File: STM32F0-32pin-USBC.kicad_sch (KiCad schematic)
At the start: 0 parts

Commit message: Added kicad_hugonlib submodule and added libs to project
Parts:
- added H1, H2, H3, H4: MountingHole, symbol Mechanical:MountingHole
- added J1: Conn_ARM_JTAG_SWD_10, symbol Connector:Conn_ARM_JTAG_SWD_10
- added J2: USB_C_Receptacle_USB2.0_16P, symbol Connector:USB_C_Receptacle_USB2.0_16P
- added U1: USBLC6-2SC6, Package_TO_SOT_SMD:SOT-23-6, symbol Power_Protection:USBLC6-2SC6
- added U2: STM32F042K6Tx, Package_QFP:LQFP-32_7x7mm_P0.8mm, symbol MCU_ST_STM32F0:STM32F042K6Tx
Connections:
- new net: J1.3 (GND), J1.5 (GND)
- new net: J2.A1 (GND), J2.A12 (GND), J2.B1 (GND), J2.B12 (GND)
- new net: J2.A4 (VBUS), J2.A9 (VBUS), J2.B4 (VBUS), J2.B9 (VBUS)

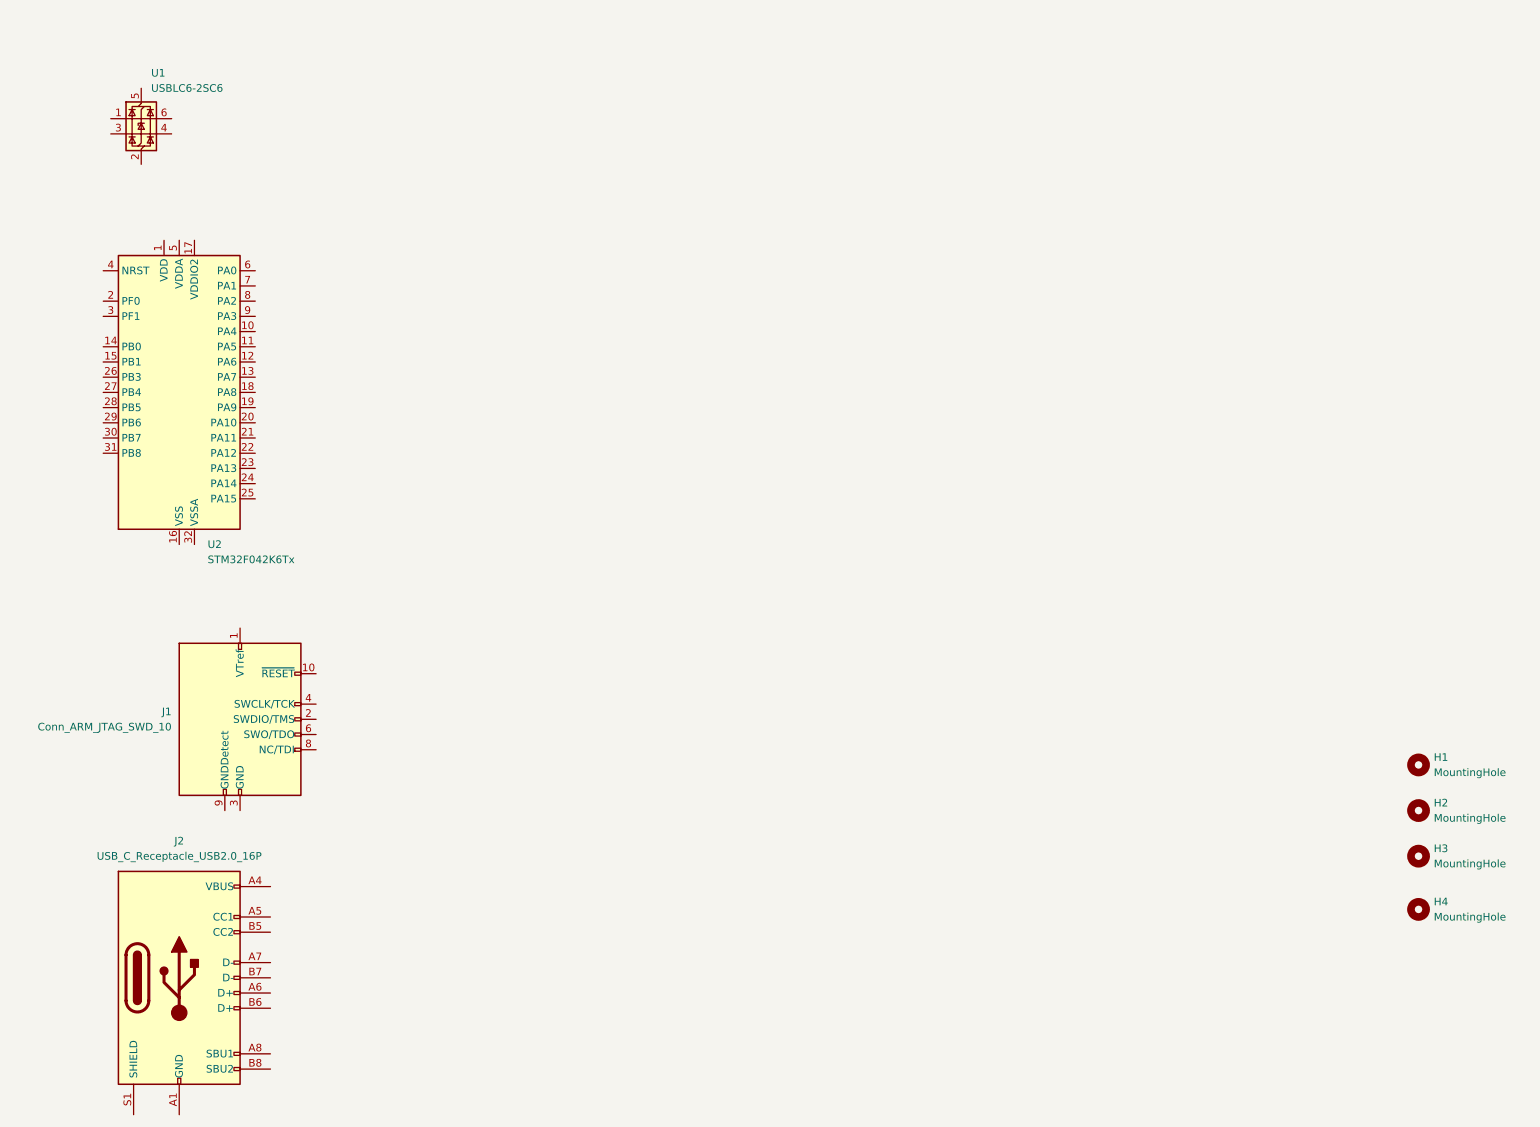
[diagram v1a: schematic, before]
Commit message: Added symbols and completed USB_and_LDO sheet
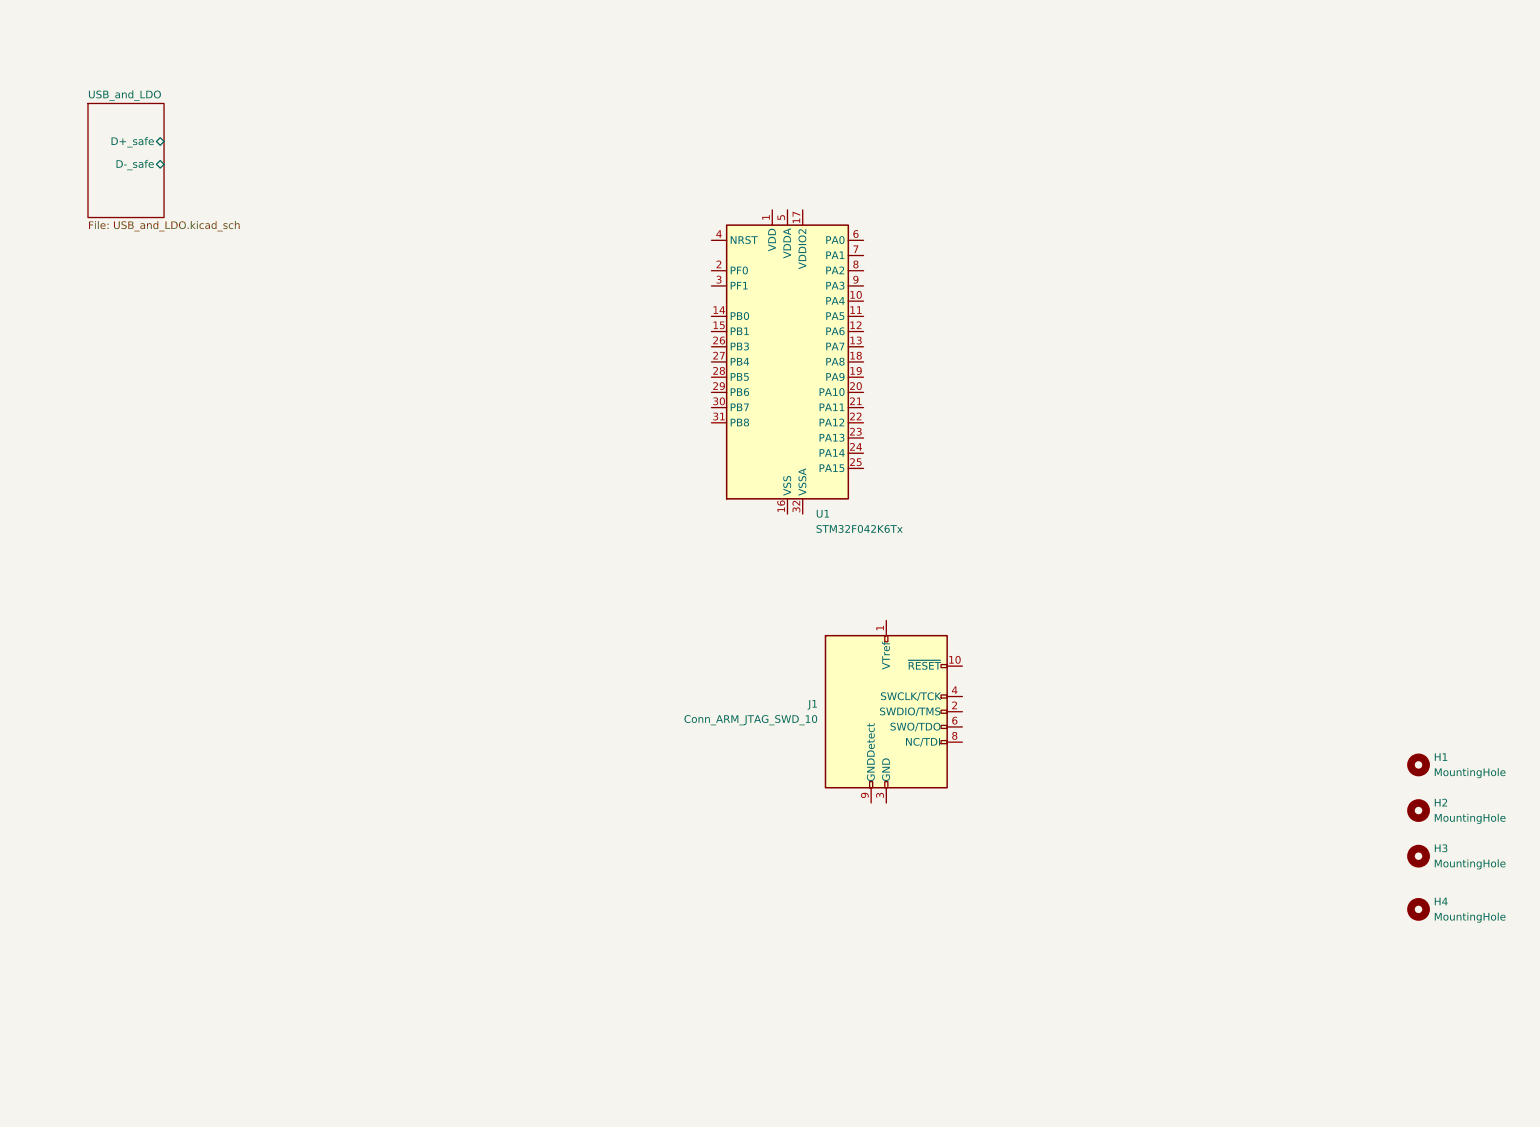
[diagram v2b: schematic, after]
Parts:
- removed J2: USB_C_Receptacle_USB2.0_16P, symbol Connector:USB_C_Receptacle_USB2.0_16P
- removed U1: USBLC6-2SC6, Package_TO_SOT_SMD:SOT-23-6, symbol Power_Protection:USBLC6-2SC6
- renumbered U2 to U1
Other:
- added sheet USB_and_LDO (USB_and_LDO.kicad_sch)
- moved on the sheet: J1, U1
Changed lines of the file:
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@@
-	)
-	(symbol
-		(lib_id "Power_Protection:USBLC6-2SC6")
-		(at 34.29 33.02 0)
-		(unit 1)
-		(exclude_from_sim no)
-		(in_bom yes)
-		(on_board yes)
-		(dnp no)
-		(fields_autoplaced yes)
-		(property "Reference" "U1"
-			(at 35.9411 25.4 0)
-			(effects
-				(font
-					(size 1.27 1.27)
-				)
-				(justify left)
-			)
-		)
-		(property "Value" "USBLC6-2SC6"
-			(at 35.9411 27.94 0)
-			(effects
-				(font
-					(size 1.27 1.27)
-				)
-				(justify left)
-			)
-		)
-		(property "Footprint" "Package_TO_SOT_SMD:SOT-23-6"
-			(at 35.56 39.37 0)
-			(effects
-				(font
-					(size 1.27 1.27)
-					(italic yes)
-				)
-				(justify left)
-				(hide yes)
-			)
-		)
-		(property "Datasheet" "https://www.st.com/resource/en/datasheet/usblc6-2.pdf"
-			(at 35.56 41.275 0)
-			(effects
-				(font
-					(size 1.27 1.27)
-				)
-				(justify left)
-				(hide yes)
-			)
-		)
-		(property "Description" "Very low capacitance ESD protection diode, 2 data-line, SOT-23-6"
-			(at 34.29 33.02 0)
-			(effects
-				(font
-					(size 1.27 1.27)
-				)
-				(hide yes)
-			)
-		)
-		(pin "4"
-		)
-		(pin "3"
-		)
-		(pin "5"
-		)
-		(pin "1"
-		)
-		(pin "2"
-		)
-		(pin "6"
-		)
-		(instances
-			(project "STM32F0-32pin-USBC"
-				(path "/442e26cf-a0b4-49b0-8670-5150c599c386"
-					(reference "U1")
-					(unit 1)
-				)
-			)
-		)
 	)
 	(symbol
@@
 	(symbol
 		(lib_id "MCU_ST_STM32F0:STM32F042K6Tx")
-		(at 40.64 78.74 0)
+		(at 142.24 73.66 0)
 		(unit 1)
 		(exclude_from_sim no)
@@
 		(dnp no)
 		(fields_autoplaced yes)
-		(property "Reference" "U2"
-			(at 45.3741 104.14 0)
+		(property "Reference" "U1"
+			(at 146.9741 99.06 0)
 			(effects
 				(font
@@
 		)
 		(property "Value" "STM32F042K6Tx"
-			(at 45.3741 106.68 0)
+			(at 146.9741 101.6 0)
 			(effects
 				(font
@@
 		)
 		(property "Footprint" "Package_QFP:LQFP-32_7x7mm_P0.8mm"
-			(at 30.48 101.6 0)
+			(at 132.08 96.52 0)
 			(effects
 				(font
@@
 		)
 		(property "Datasheet" "https://www.st.com/resource/en/datasheet/stm32f042k6.pdf"
-			(at 40.64 78.74 0)
+			(at 142.24 73.66 0)
 			(effects
 				(font
@@
 		)
 		(property "Description" "STMicroelectronics Arm Cortex-M0 MCU, 32KB flash, 6KB RAM, 48 MHz, 2.0-3.6V, 26 GPIO, LQFP32"
-			(at 40.64 78.74 0)
+			(at 142.24 73.66 0)
 			(effects
 				(font
@@
 			(project "STM32F0-32pin-USBC"
 				(path "/442e26cf-a0b4-49b0-8670-5150c599c386"
-					(reference "U2")
+					(reference "U1")
 					(unit 1)
 				)
@@
 	(symbol
 		(lib_id "Connector:Conn_ARM_JTAG_SWD_10")
-		(at 50.8 133.35 0)
+		(at 158.75 132.08 0)
 		(unit 1)
 		(exclude_from_sim no)
@@
 		(fields_autoplaced yes)
 		(property "Reference" "J1"
-			(at 39.37 132.0799 0)
+			(at 147.32 130.8099 0)
 			(effects
 				(font
@@
 		)
 		(property "Value" "Conn_ARM_JTAG_SWD_10"
-			(at 39.37 134.6199 0)
+			(at 147.32 133.3499 0)
 			(effects
 				(font
@@
 		)
 		(property "Footprint" ""
-			(at 50.8 133.35 0)
+			(at 158.75 132.08 0)
 			(effects
 				(font
@@
 		)
 		(property "Datasheet" "http://infocenter.arm.com/help/topic/com.arm.doc.ddi0314h/DDI0314H_coresight_components_trm.pdf"
-			(at 41.91 165.1 90)
+			(at 149.86 163.83 90)
 			(effects
 				(font
@@
 		)
 		(property "Description" "Cortex Debug Connector, standard ARM Cortex-M SWD and JTAG interface"
-			(at 50.8 133.35 0)
+			(at 158.75 132.08 0)
 			(effects
 				(font
@@
 				(path "/442e26cf-a0b4-49b0-8670-5150c599c386"
 					(reference "J1")
-					(unit 1)
-				)
-			)
-		)
-	)
-	(symbol
-		(lib_id "Connector:USB_C_Receptacle_USB2.0_16P")
-		(at 40.64 176.53 0)
-		(unit 1)
-		(exclude_from_sim no)
-		(in_bom yes)
-		(on_board yes)
-		(dnp no)
-		(fields_autoplaced yes)
-		(property "Reference" "J2"
-			(at 40.64 153.67 0)
-			(effects
-				(font
-					(size 1.27 1.27)
-				)
-			)
-		)
-		(property "Value" "USB_C_Receptacle_USB2.0_16P"
-			(at 40.64 156.21 0)
-			(effects
-				(font
-					(size 1.27 1.27)
-				)
-			)
-		)
-		(property "Footprint" ""
-			(at 44.45 176.53 0)
-			(effects
-				(font
-					(size 1.27 1.27)
-				)
-				(hide yes)
-			)
-		)
-		(property "Datasheet" "https://www.usb.org/sites/default/files/documents/usb_type-c.zip"
-			(at 44.45 176.53 0)
-			(effects
-				(font
-					(size 1.27 1.27)
-				)
-				(hide yes)
-			)
-		)
-		(property "Description" "USB 2.0-only 16P Type-C Receptacle connector"
-			(at 40.64 176.53 0)
-			(effects
-				(font
-					(size 1.27 1.27)
-				)
-				(hide yes)
-			)
-		)
-		(pin "A9"
-		)
-		(pin "A8"
-		)
-		(pin "A1"
-		)
-		(pin "B9"
-		)
-		(pin "B6"
-		)
-		(pin "B12"
-		)
-		(pin "A12"
-		)
-		(pin "B1"
-		)
-		(pin "A6"
-		)
-		(pin "B7"
-		)
-		(pin "A4"
-		)
-		(pin "A5"
-		)
-		(pin "B8"
-		)
-		(pin "B5"
-		)
-		(pin "S1"
-		)
-		(pin "A7"
-		)
-		(pin "B4"
-		)
-		(instances
-			(project "STM32F0-32pin-USBC"
-				(path "/442e26cf-a0b4-49b0-8670-5150c599c386"
-					(reference "J2")
 					(unit 1)
 				)
@@
 				)
 			)
+		)
+	)
+	(sheet
+		(at 25.4 30.48)
+		(size 12.7 19.05)
+		(fields_autoplaced yes)
+		(stroke
+			(width 0.1524)
+			(type solid)
+		)
+		(fill
+			(color 0 0 0 0.0000)
+		)
+		(property "Sheetname" "USB_and_LDO"
+			(at 25.4 29.7684 0)
+			(effects
+				(font
+					(size 1.27 1.27)
+				)
+				(justify left bottom)
+			)
+		)
+		(property "Sheetfile" "USB_and_LDO.kicad_sch"
+			(at 25.4 50.1146 0)
+			(effects
+				(font
+					(size 1.27 1.27)
+				)
+				(justify left top)
+			)
+		)
+		(pin "D-_safe" bidirectional
+			(at 38.1 40.64 0)
+			(effects
+				(font
+					(size 1.27 1.27)
+				)
+				(justify right)
+			)
+		)
+		(pin "D+_safe" bidirectional
+			(at 38.1 36.83 0)
+			(effects
+				(font
+					(size 1.27 1.27)
+				)
+				(justify right)
+			)
+		)
+		(instances
+			(project "STM32F0-32pin-USBC"
+				(path "/442e26cf-a0b4-49b0-8670-5150c599c386"
+					(page "2")
+				)
+			)

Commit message: work on schematic
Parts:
- added C4, C5, C6: 100n, symbol Device:C
- added D1, D2, D3, D4: LED, symbol Device:LED
- added R4, R5, R6, R7: R_US, symbol Device:R_US
- added U4: MCP2221AxSL, Package_SO:SOIC-14_3.9x8.7mm_P1.27mm, symbol Interface_USB:MCP2221AxSL
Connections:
- net USB_and_LDO/D+_safe: now also U4.13 (D+)
- net USB_and_LDO/D-_safe: now also U4.12 (D-)
- net +3.3V: now reaches U1.1 (VDD)
- net +3.3V: now also J1.1 (VTref), U1.17 (VDDIO2), U1.5 (VDDA), C4.1, C5.1, C6.1, U4.1 (VDD), U4.11 (VUSB)
- net PA4: now reaches U1.10 (PA4)
- net PA5: now reaches U1.11 (PA5)
- net PA6: now reaches U1.12 (PA6)
- net PA7: now reaches U1.13 (PA7)
- net PB0: now reaches U1.14 (PB0)
- net PB0: now also D1.2 (A)
- net PB1: now reaches U1.15 (PB1)
- net PB1: now also D2.2 (A)
- net GND: now reaches U1.16 (VSS)
- net GND: now also J1.3 (GND), J1.5 (GND), J1.9 (GNDDetect), U1.32 (VSSA), C4.2, C5.2, C6.2, R4.2, R5.2, R6.2, R7.2, U4.14 (VSS)
- net PA8: now reaches U1.18 (PA8)
- net PA9: now reaches U1.19 (PA9)
- net PA9: now also U4.5 (URx)
- net PF0: now reaches U1.2 (PF0)
- net PA10: now reaches U1.20 (PA10)
- net PA10: now also U4.6 (UTx)
- net PA11: now reaches U1.21 (PA11)
- net PA12: now reaches U1.22 (PA12)
- net PA13: now reaches U1.23 (PA13)
- net PA13: now also J1.2 (SWDIO/TMS)
- net PA14: now reaches U1.24 (PA14)
- net PA14: now also J1.4 (SWCLK/TCK)
- net PA15: now reaches U1.25 (PA15)
- net PB3: now reaches U1.26 (PB3)
- net PB3: now also D3.2 (A)
- net PB4: now reaches U1.27 (PB4)
- net PB4: now also D4.2 (A)
- net PB5: now reaches U1.28 (PB5)
- net PB6: now reaches U1.29 (PB6)
- net PF1: now reaches U1.3 (PF1)
- net PB7: now reaches U1.30 (PB7)
- net PB8: now reaches U1.31 (PB8)
- net NRESET: now reaches U1.4 (NRST)
- net NRESET: now also J1.10 (~{RESET})
- net PA0: now reaches U1.6 (PA0)
- net PA1: now reaches U1.7 (PA1)
- net PA2: now reaches U1.8 (PA2)
- net PA3: now reaches U1.9 (PA3)
- new net: D1.1 (K), R4.1
- new net: D2.1 (K), R5.1
- new net: D4.1 (K), R7.1
- new net: D3.1 (K), R6.1
- no-connect marks 0 -> 9
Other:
- note added: "PA9 is USART1_TX PA10 is USART1_RX"
- note added: "SWDIO is PA13 SWCLK is PA14 According to https://www.st.com/resource/en/reference_manual/rm0091-stm32f0x1stm32f0x2stm32f0x8-advanced-armbased-32bit-mcus-stmicroelectronics.pdf"
